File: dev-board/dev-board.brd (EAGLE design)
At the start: 49.2 x 64.8 mm, 38 parts, among them J1 12401832E402A, U1 STM32F103RET6, U2 AT24C64BN-10SU-2.7, U3 FT232RL, U4 MCP2551, U5 LM1117IMP-3.3, X1 8MHz

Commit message: Fix 5V plane problem in dev-board pcb design
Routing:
- net +5V: track 121.6 -> 107.4 mm
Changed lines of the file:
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@@
 <layer number="13" name="Route13" color="4" fill="5" visible="no" active="no"/>
 <layer number="14" name="Route14" color="1" fill="6" visible="no" active="no"/>
-<layer number="15" name="Route15" color="23" fill="1" visible="no" active="yes"/>
+<layer number="15" name="Route15" color="23" fill="1" visible="yes" active="yes"/>
 <layer number="16" name="Bottom" color="1" fill="1" visible="no" active="yes"/>
 <layer number="17" name="Pads" color="2" fill="1" visible="yes" active="yes"/>
@@
 <wire x1="-1.27" y1="6.604" x2="-1.27" y2="38.354" width="0.3048" layer="15"/>
 <contactref element="JP1" pad="1"/>
-<wire x1="36.322" y1="4.572" x2="27.432" y2="13.462" width="0.3048" layer="15"/>
-<wire x1="27.432" y1="13.462" x2="27.432" y2="15.113" width="0.3048" layer="15"/>
+<wire x1="27.4456" y1="11.176" x2="36.322" y2="4.572" width="0" layer="19" extent="1-1"/>
 </signal>
 <signal name="GND">

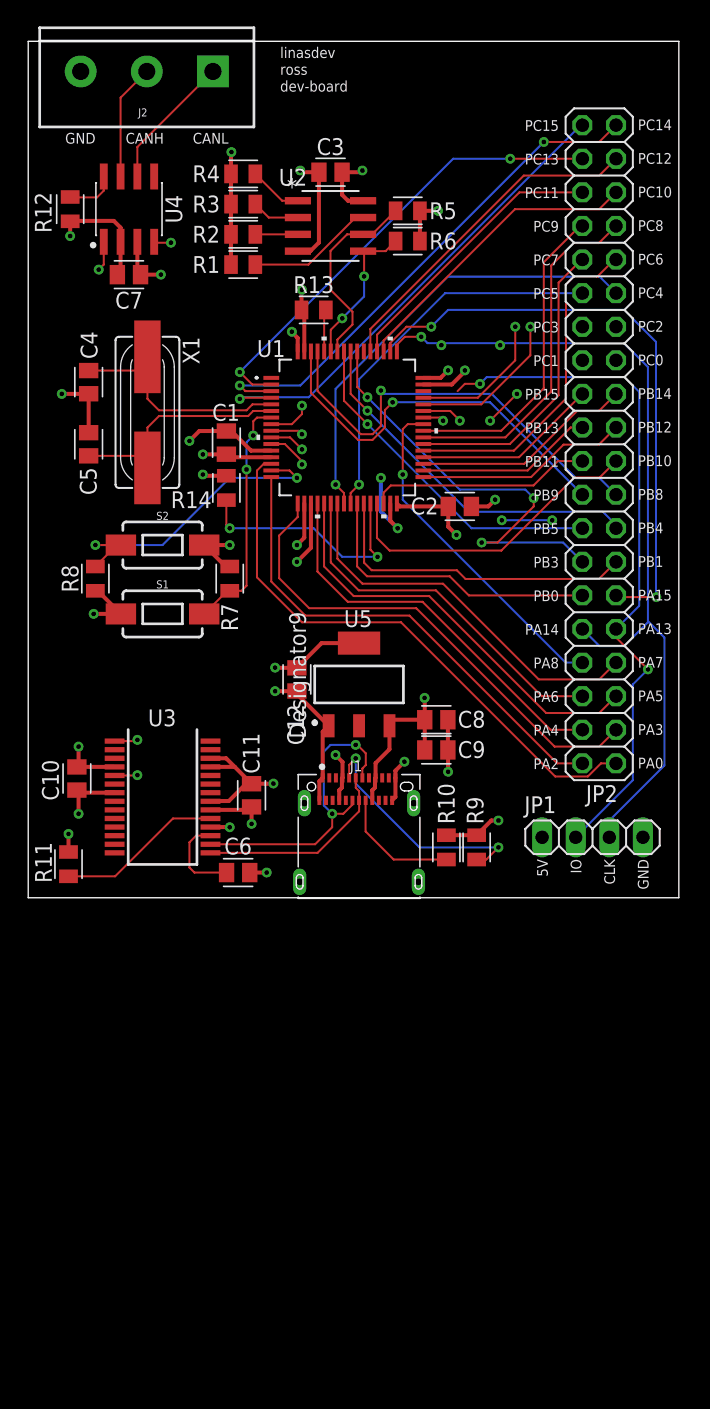
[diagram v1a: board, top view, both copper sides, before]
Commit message: Improve dev-board design further
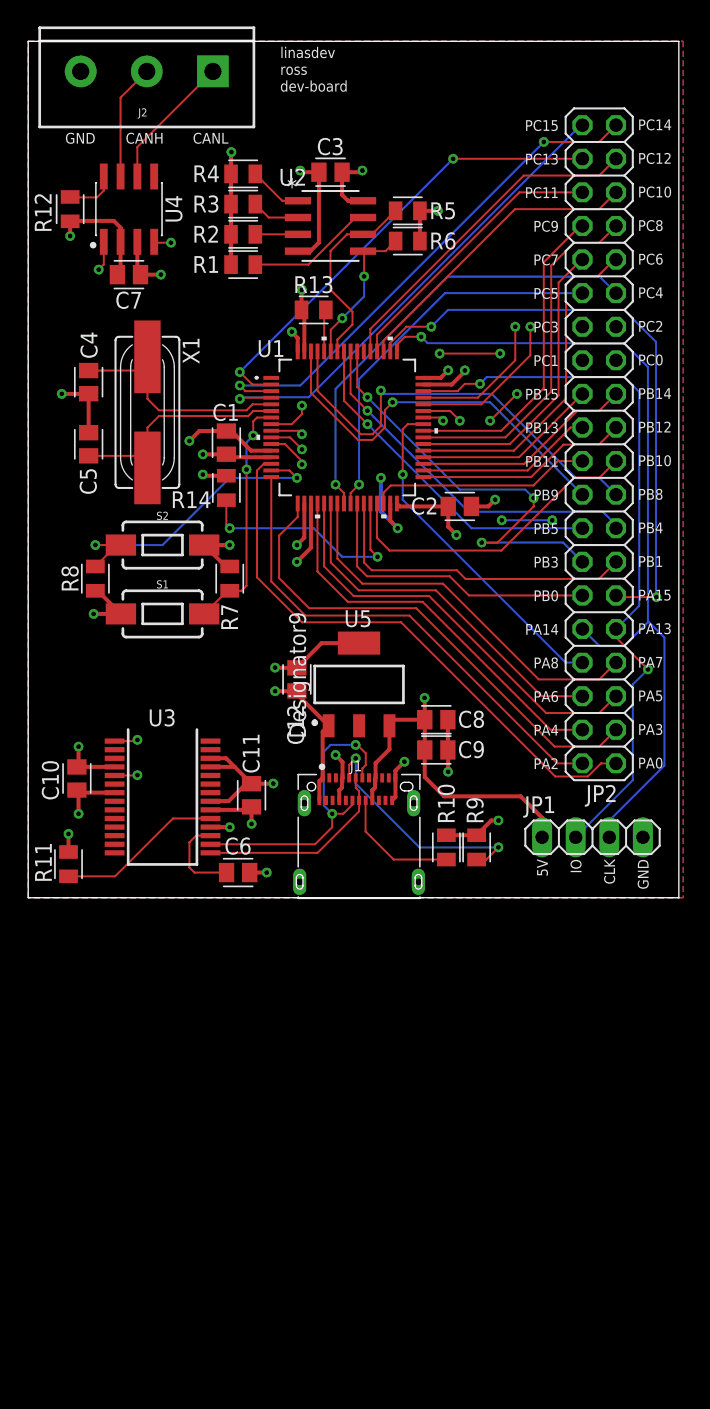
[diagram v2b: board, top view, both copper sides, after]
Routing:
- net +5V: track 107.4 -> 121.0 mm
- net PC0: track 24.9 -> 29.5 mm
- net SWDIO: track 52.3 -> 54.9 mm
- net SWCLK: track 64.3 -> 64.8 mm
- added copper zone on layer 1, net GND
- added copper zone on layer 16, net GND
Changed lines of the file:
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@@
 <layers>
 <layer number="1" name="Top" color="4" fill="1" visible="yes" active="yes"/>
-<layer number="2" name="Route2" color="16" fill="1" visible="no" active="yes"/>
+<layer number="2" name="Route2" color="16" fill="1" visible="yes" active="yes"/>
 <layer number="3" name="Route3" color="4" fill="3" visible="no" active="no"/>
 <layer number="4" name="Route4" color="1" fill="4" visible="no" active="no"/>
@@
 <layer number="14" name="Route14" color="1" fill="6" visible="no" active="no"/>
 <layer number="15" name="Route15" color="23" fill="1" visible="yes" active="yes"/>
-<layer number="16" name="Bottom" color="1" fill="1" visible="no" active="yes"/>
+<layer number="16" name="Bottom" color="1" fill="1" visible="yes" active="yes"/>
 <layer number="17" name="Pads" color="2" fill="1" visible="yes" active="yes"/>
 <layer number="18" name="Vias" color="2" fill="1" visible="yes" active="yes"/>
@@
 <layer number="20" name="Dimension" color="24" fill="1" visible="yes" active="yes"/>
 <layer number="21" name="tPlace" color="7" fill="1" visible="yes" active="yes"/>
-<layer number="22" name="bPlace" color="7" fill="1" visible="no" active="yes"/>
+<layer number="22" name="bPlace" color="7" fill="1" visible="yes" active="yes"/>
 <layer number="23" name="tOrigins" color="15" fill="1" visible="yes" active="yes"/>
-<layer number="24" name="bOrigins" color="15" fill="1" visible="no" active="yes"/>
+<layer number="24" name="bOrigins" color="15" fill="1" visible="yes" active="yes"/>
 <layer number="25" name="tNames" color="7" fill="1" visible="yes" active="yes"/>
-<layer number="26" name="bNames" color="7" fill="1" visible="no" active="yes"/>
+<layer number="26" name="bNames" color="7" fill="1" visible="yes" active="yes"/>
 <layer number="27" name="tValues" color="7" fill="1" visible="no" active="yes"/>
 <layer number="28" name="bValues" color="7" fill="1" visible="no" active="yes"/>
@@
 <layer number="38" name="bTest" color="7" fill="1" visible="no" active="yes"/>
 <layer number="39" name="tKeepout" color="4" fill="11" visible="yes" active="yes"/>
-<layer number="40" name="bKeepout" color="1" fill="11" visible="no" active="yes"/>
+<layer number="40" name="bKeepout" color="1" fill="11" visible="yes" active="yes"/>
 <layer number="41" name="tRestrict" color="4" fill="10" visible="yes" active="yes"/>
-<layer number="42" name="bRestrict" color="1" fill="10" visible="no" active="yes"/>
+<layer number="42" name="bRestrict" color="1" fill="10" visible="yes" active="yes"/>
 <layer number="43" name="vRestrict" color="2" fill="10" visible="no" active="yes"/>
 <layer number="44" name="Drills" color="7" fill="1" visible="no" active="yes"/>
@@
 <layer number="50" name="dxf" color="7" fill="1" visible="no" active="no"/>
 <layer number="51" name="tDocu" color="7" fill="1" visible="yes" active="yes"/>
-<layer number="52" name="bDocu" color="7" fill="1" visible="no" active="yes"/>
+<layer number="52" name="bDocu" color="7" fill="1" visible="yes" active="yes"/>
 <layer number="53" name="tGND_GNDA" color="7" fill="9" visible="no" active="no"/>
 <layer number="54" name="bGND_GNDA" color="1" fill="9" visible="no" active="no"/>
@@
 <wire x1="-1.27" y1="6.604" x2="-1.27" y2="38.354" width="0.3048" layer="15"/>
 <contactref element="JP1" pad="1"/>
-<wire x1="27.4456" y1="11.176" x2="36.322" y2="4.572" width="0" layer="19" extent="1-1"/>
+<wire x1="27.4456" y1="11.176" x2="27.4456" y2="9.1304" width="0.3048" layer="1"/>
+<wire x1="27.4456" y1="9.1304" x2="28.908" y2="7.668" width="0.3048" layer="1"/>
+<wire x1="36.322" y1="4.572" x2="36.322" y2="6.0459125" width="0.3048" layer="1"/>
+<wire x1="36.322" y1="6.0459125" x2="34.6999125" y2="7.668" width="0.3048" layer="1"/>
+<wire x1="28.908" y1="7.668" x2="34.6999125" y2="7.668" width="0.3048" layer="1"/>
 </signal>
 <signal name="GND">
@@
 <wire x1="12.4284" y1="10.545" x2="13.0784" y2="9.895" width="0.3048" layer="1"/>
 <contactref element="JP1" pad="4"/>
+<polygon width="0.3048" layer="1">
+<vertex x="-2.54" y="64.77"/>
+<vertex x="46.99" y="64.77"/>
+<vertex x="46.99" y="0"/>
+<vertex x="-2.54" y="0"/>
+</polygon>
+<polygon width="0.3048" layer="16">
+<vertex x="-2.54" y="64.77"/>
+<vertex x="46.99" y="64.77"/>
+<vertex x="46.99" y="0"/>
+<vertex x="-2.54" y="0"/>
+</polygon>
 </signal>
 <signal name="N$14">
@@
 <via x="13.462" y="39.751" extent="1-16" drill="0.35"/>
 <wire x1="13.462" y1="39.751" x2="29.591" y2="55.88" width="0.1524" layer="16"/>
-<wire x1="29.591" y1="55.88" x2="33.909" y2="55.88" width="0.1524" layer="16"/>
-<via x="33.909" y="55.88" extent="1-16" drill="0.35"/>
-<wire x1="33.909" y1="55.88" x2="39.37" y2="55.88" width="0.1524" layer="1"/>
+<via x="29.591" y="55.88" extent="1-16" drill="0.35"/>
+<wire x1="29.591" y1="55.88" x2="39.37" y2="55.88" width="0.1524" layer="1"/>
 </signal>
 <signal name="PC14">
@@
 <wire x1="18.161" y1="36.576" x2="18.161" y2="37.211" width="0.1524" layer="1"/>
 <via x="18.161" y="37.211" extent="1-16" drill="0.35"/>
-<wire x1="18.161" y1="37.211" x2="22.733" y2="41.783" width="0.1524" layer="2"/>
-<wire x1="40.767" y1="41.783" x2="41.91" y2="40.64" width="0.1524" layer="2"/>
-<wire x1="22.733" y1="41.783" x2="28.702" y2="41.783" width="0.1524" layer="2"/>
-<via x="28.702" y="41.783" extent="1-16" drill="0.35"/>
-<wire x1="33.147" y1="41.783" x2="40.767" y2="41.783" width="0.1524" layer="2"/>
-<via x="33.147" y="41.783" extent="1-16" drill="0.35"/>
-<wire x1="28.702" y1="41.783" x2="33.147" y2="41.783" width="0" layer="19" extent="1-1"/>
+<wire x1="18.161" y1="37.211" x2="22.098" y2="41.148" width="0.1524" layer="2"/>
+<wire x1="40.64" y1="41.91" x2="41.91" y2="40.64" width="0.1524" layer="2"/>
+<wire x1="22.098" y1="41.148" x2="28.575" y2="41.148" width="0.1524" layer="2"/>
+<via x="28.575" y="41.148" extent="1-16" drill="0.35"/>
+<wire x1="40.64" y1="41.91" x2="33.909" y2="41.91" width="0.1524" layer="2"/>
+<wire x1="33.147" y1="41.148" x2="33.909" y2="41.91" width="0.1524" layer="2"/>
+<via x="33.147" y="41.148" extent="1-16" drill="0.35"/>
+<wire x1="28.575" y1="41.148" x2="33.147" y2="41.148" width="0.1524" layer="1"/>
 </signal>
 <signal name="PC1">
@@
 <via x="18.161" y="32.766" extent="1-16" drill="0.35"/>
 <wire x1="18.161" y1="32.766" x2="21.6535" y2="29.2735" width="0.1524" layer="2"/>
-<wire x1="21.6535" y1="29.2735" x2="21.6916" y2="29.2354" width="0.1524" layer="2"/>
 <wire x1="42.574325" y1="29.2354" x2="44.2978" y2="30.958875" width="0.1524" layer="2"/>
 <wire x1="42.574325" y1="44.4246" x2="40.610675" y2="44.4246" width="0.1524" layer="2"/>
@@
 <contactref element="U1" pad="46"/>
 <contactref element="JP2" pad="9"/>
-<wire x1="30.48" y1="38.862" x2="29.928" y2="38.31" width="0.1524" layer="1"/>
+<wire x1="29.928" y1="38.31" x2="30.48" y2="38.862" width="0.1524" layer="1"/>
 <wire x1="30.48" y1="38.862" x2="31.623" y2="38.862" width="0.1524" layer="1"/>
 <via x="31.623" y="38.862" extent="1-16" drill="0.35"/>
@@
 <wire x1="41.91" y1="19.685" x2="41.91" y2="20.32" width="0.1524" layer="1"/>
 <wire x1="43.18" y1="8.89" x2="43.18" y2="16.129" width="0.1524" layer="16"/>
-<wire x1="29.928" y1="38.31" x2="27.34" y2="38.31" width="0" layer="19" extent="1-1"/>
+<wire x1="27.34" y1="38.31" x2="29.928" y2="38.31" width="0.1524" layer="1"/>
 </signal>
 <signal name="SWCLK">
 <contactref element="U1" pad="49"/>
 <contactref element="JP2" pad="10"/>
-<wire x1="25.94" y1="42.418" x2="25.34" y2="41.818" width="0.1524" layer="1"/>
+<wire x1="25.94" y1="42.418" x2="25.416" y2="41.894" width="0.1524" layer="1"/>
 <wire x1="25.94" y1="42.418" x2="27.178" y2="42.418" width="0.1524" layer="1"/>
 <via x="27.178" y="42.418" extent="1-16" drill="0.35"/>
@@
 <wire x1="44.323" y1="20.828" x2="44.323" y2="20.92415" width="0.1524" layer="16"/>
 <wire x1="42.5196" y1="19.0246" x2="44.323" y2="20.828" width="0.1524" layer="16"/>
-<wire x1="25.34" y1="41.818" x2="25.34" y2="41.31" width="0" layer="19" extent="1-1"/>
+<wire x1="25.416" y1="41.894" x2="25.416" y2="41.386" width="0.1524" layer="1"/>
+<wire x1="25.416" y1="41.386" x2="25.34" y2="41.31" width="0.1524" layer="1"/>
 </signal>
 </signals>

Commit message: Remove leftover stuff
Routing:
- net GND: track 108.6 -> 104.2 mm, vias 21 -> 20
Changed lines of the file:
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@@
 <wire x1="18.34" y1="27.23" x2="17.78" y2="26.67" width="0.3048" layer="1"/>
 <via x="17.78" y="26.67" extent="1-16" drill="0.35"/>
-<via x="24.13" y="31.75" extent="1-16" drill="0.35"/>
-<wire x1="25.4" y1="27.94" x2="24.13" y2="29.21" width="0.3048" layer="16"/>
-<wire x1="24.13" y1="29.21" x2="24.13" y2="31.75" width="0.3048" layer="16"/>
 <wire x1="15.84" y1="33.81" x2="14.3094" y2="33.81" width="0.3048" layer="1"/>
 <wire x1="14.3094" y1="33.81" x2="12.827" y2="35.2924" width="0.3048" layer="1"/>

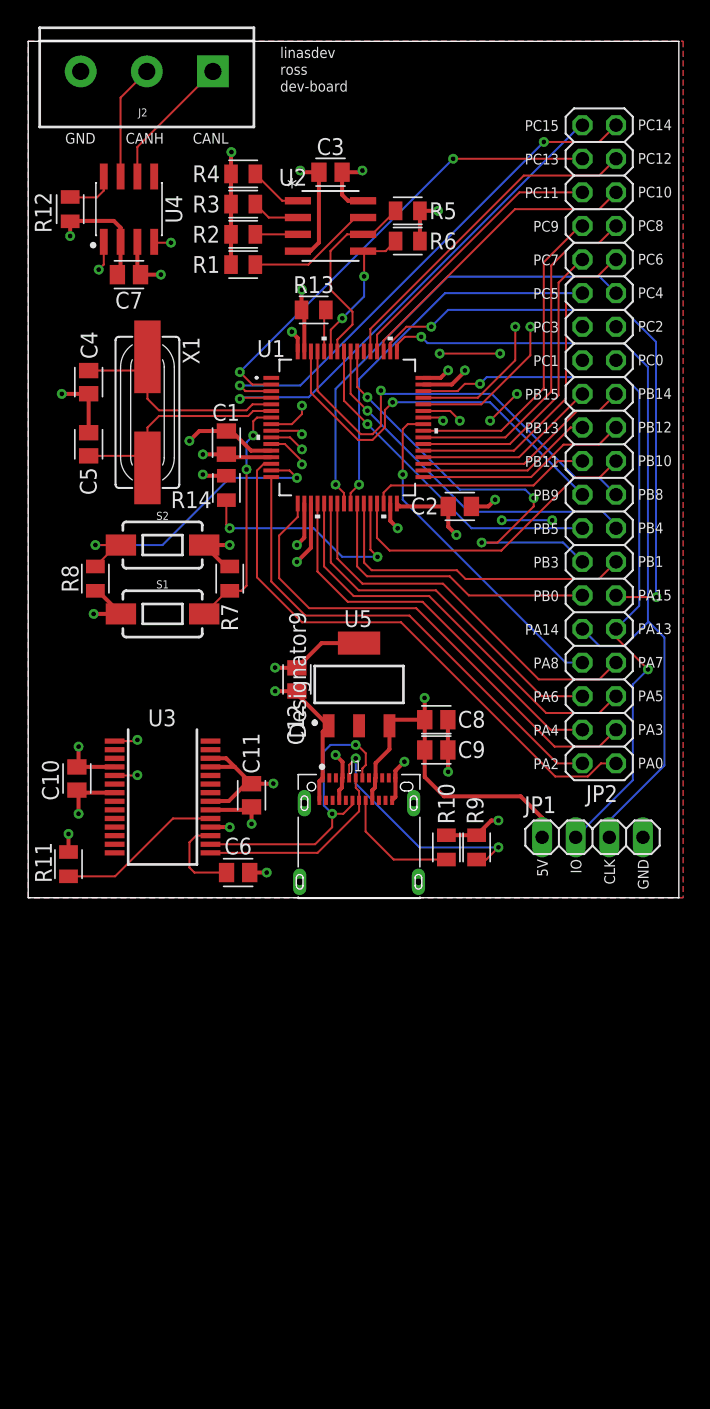
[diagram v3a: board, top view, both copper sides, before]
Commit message: Improve dev-board top layer ground plane
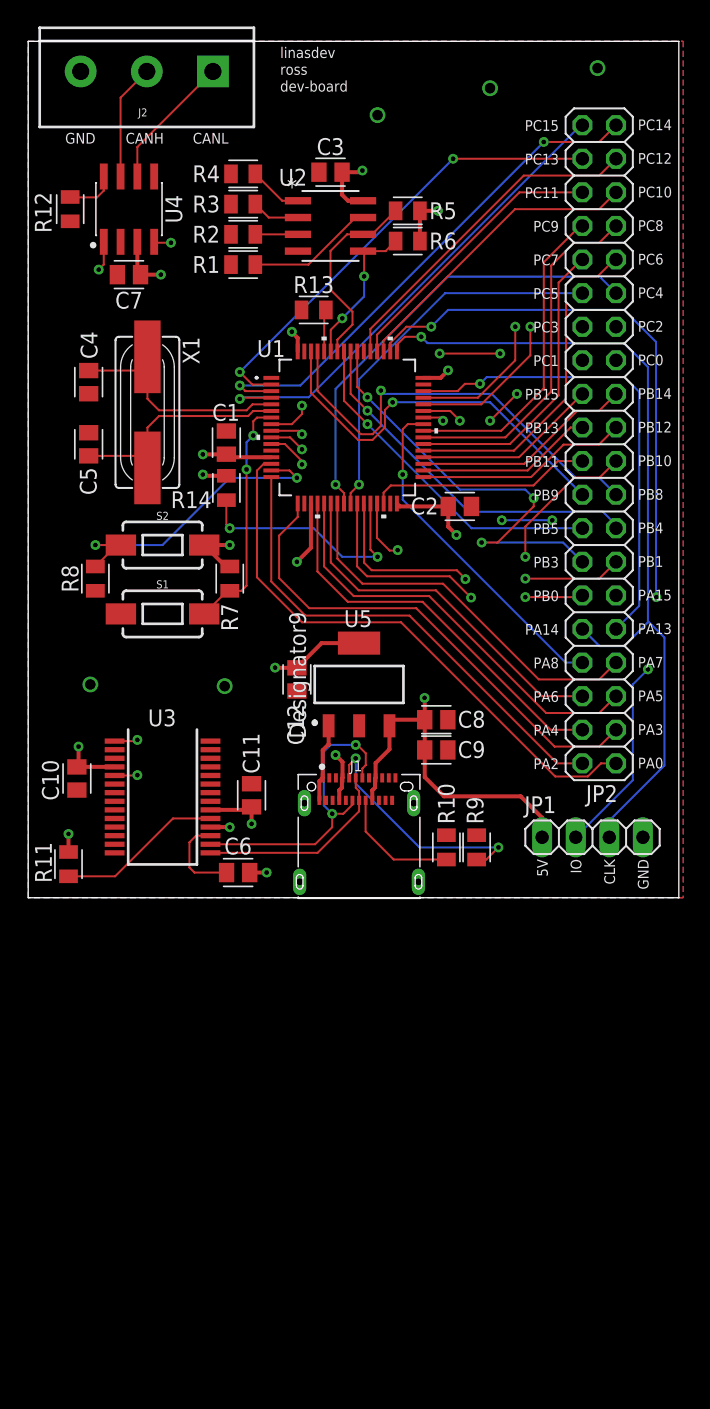
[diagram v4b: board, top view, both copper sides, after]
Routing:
- net GND: track 104.2 -> 11.4 mm, vias 20 -> 8
- net PB10: track 23.9 -> 25.6 mm, vias 0 -> 2
- net PB0: track 22.7 -> 22.8 mm, vias 0 -> 2
- net PB1: vias 0 -> 2

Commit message: Clean up dev-board schematic
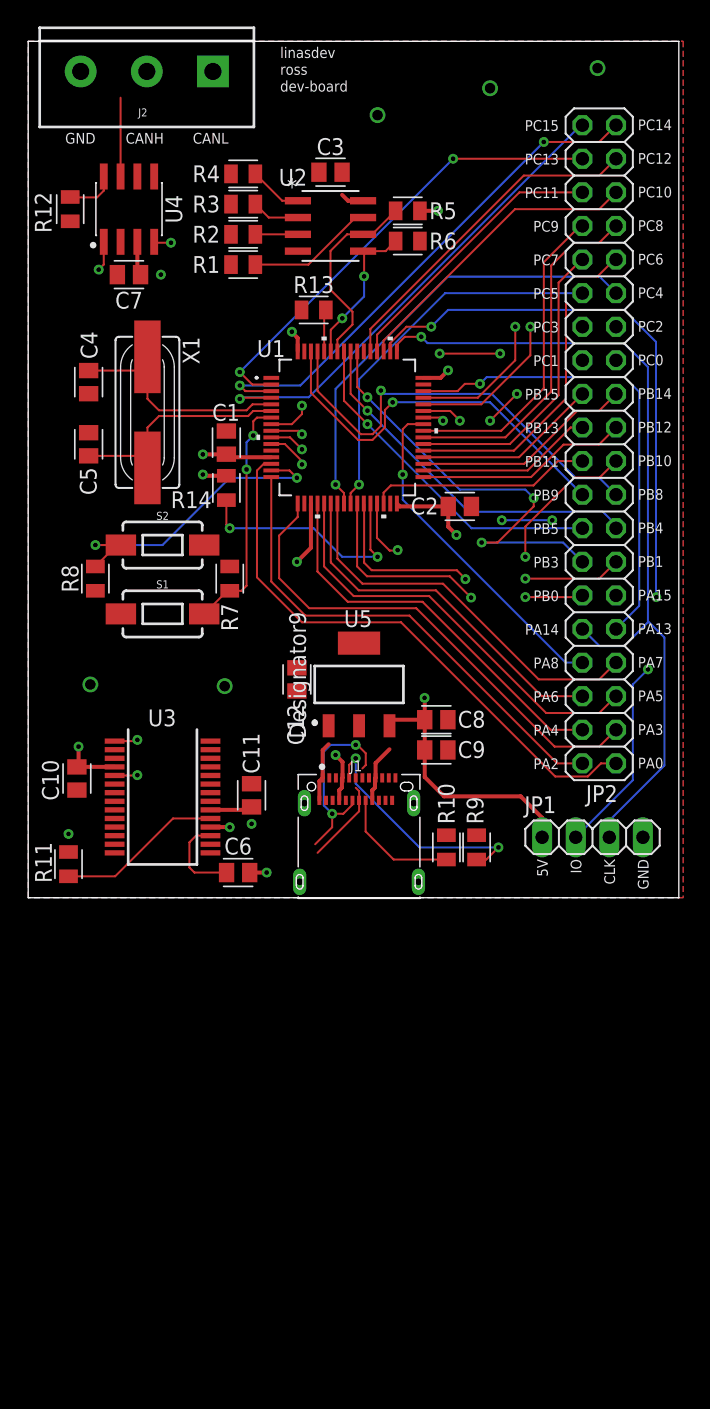
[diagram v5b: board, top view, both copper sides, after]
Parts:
- R1, R11, R13, R14, R2, R3, R4, R7, R8: value 6K8 -> 10K
- R5, R6: value 6K8 -> 4k7
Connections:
- net N$14 renamed USBDP
- net N$16 renamed USBDM
- net N$7 renamed CANH
- net N$8 renamed CANL
- removed net OUT_2: U5.2
- net +3V3: now also C3.1, U5.2; no longer C3.2
- net GND: now also C3.2, J1.SH1, J1.SH2, J1.SH3, J1.SH4; no longer C3.1
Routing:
- net +3V3: track 45.1 -> 28.2 mm, vias 10 -> 7
- net CANL: track 10.3 -> 0.00 mm
- net USBDP: track 15.2 -> 6.34 mm
- net USBDM: track 23.5 -> 14.8 mm
- net +5V: track 121.0 -> 114.0 mm
- net CANH: track 8.77 -> 5.96 mm
- net GND: track 11.4 -> 9.12 mm
